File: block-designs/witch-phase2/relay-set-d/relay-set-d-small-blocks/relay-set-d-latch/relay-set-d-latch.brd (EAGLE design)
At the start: 98.8 x 51.6 mm, 58 parts, among them IC1 74LVC1G125DBV, IC10 741G175, IC11 74LVC1G17DBV, IC12 74LVC1G17DBV, IC17 74LVC1G14DBV, IC2 74LVC1G125DBV, IC3 74LVC1G125DBV, IC4 74LVC1G125DBV, IC5 74LVC1G125DBV, IC6 741G175, IC7 741G175, IC8 741G175, IC9 741G175, Q1 MMBT2907ALT1SMD, Q2 MMBT2907ALT1SMD

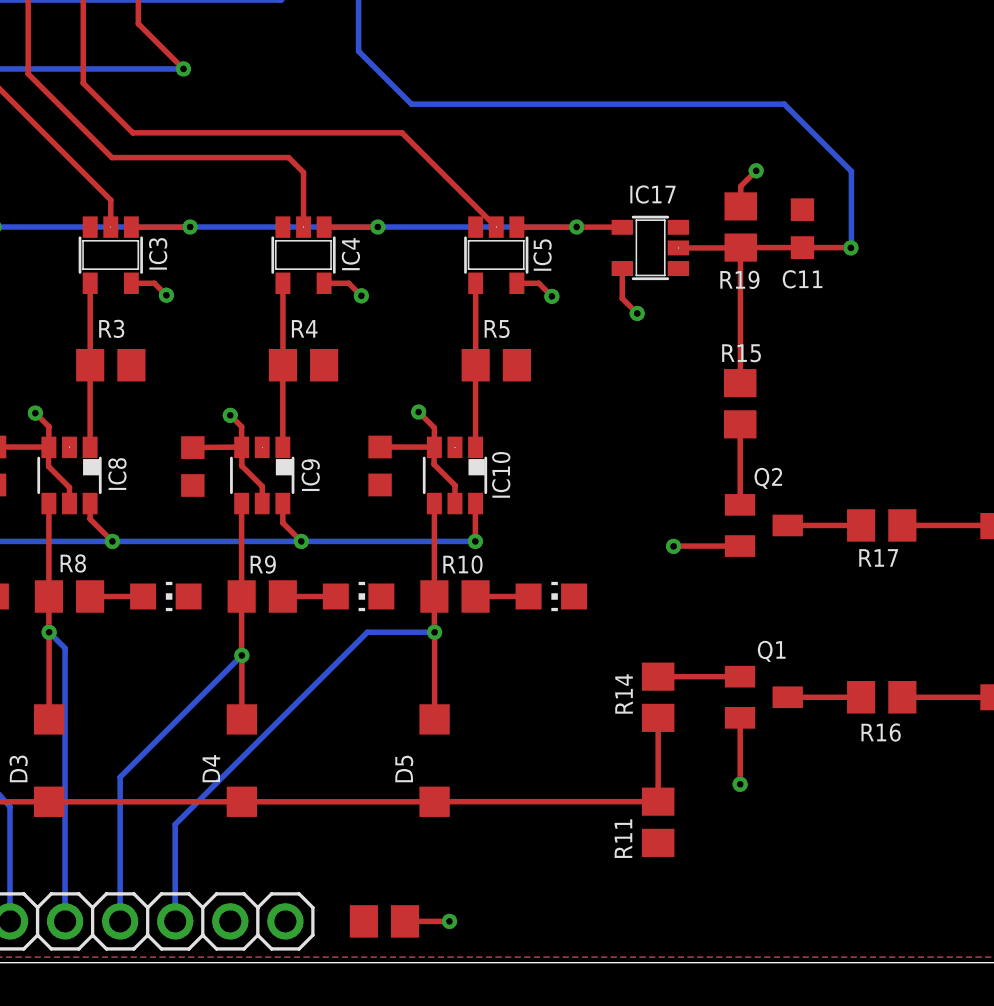
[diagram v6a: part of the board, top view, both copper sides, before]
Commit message: rework of cabling for reset, exec, power, and key-up detection
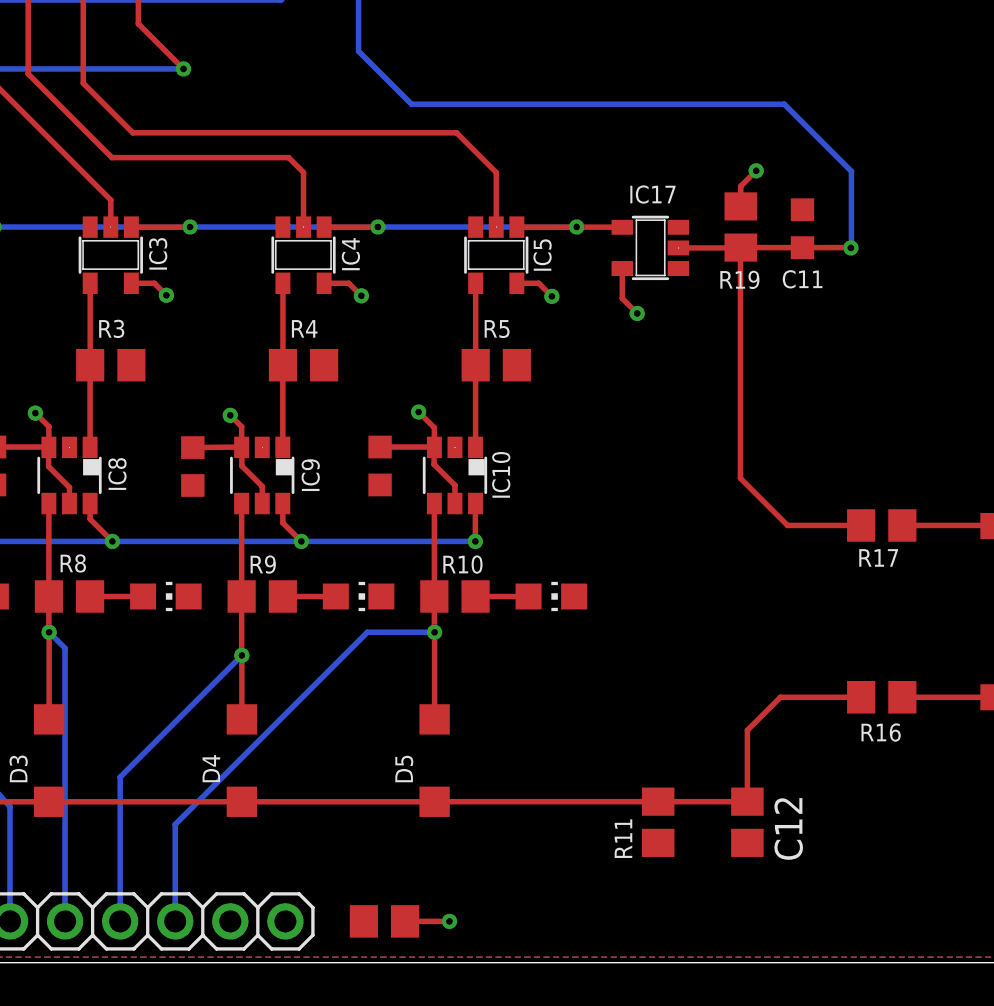
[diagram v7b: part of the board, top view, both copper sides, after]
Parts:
- removed Q1, Q2: MMBT2907ALT1SMD, transistor-pnp:SOT23-BEC
- removed R14, R15: (no value), resistor:R0805
- added C12: (no value), resistor:C0805
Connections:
- removed net N$16: Q2.B, R15.1
- removed net N$23: Q2.C, R17.1
- removed net N$25: Q1.B, R14.1
- removed net N$26: Q1.C, R16.1
- net DATA: now also C12.1, R16.1; no longer R14.2
- net GND: now also C12.2
- net SELECT: now also R17.1; no longer R15.2
- net VCC: no longer Q1.E, Q2.E
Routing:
- net SELECT: track 50.4 -> 61.3 mm
- net DATA: track 57.0 -> 66.4 mm
- net VCC: track 84.5 -> 78.3 mm, vias 18 -> 16
- net N$25: track 3.78 -> 0.00 mm
- net N$16: track 3.72 -> 0.00 mm
- net N$26: track 3.39 -> 0.00 mm
- net N$23: track 3.39 -> 0.00 mm
- net DE_IN: track 30.9 -> 32.4 mm
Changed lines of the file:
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@@
 <attribute name="VALUE" x="90.0176" y="17.6022" size="1.27" layer="27"/>
-</element>
-<element name="Q2" library="transistor-pnp" package="SOT23-BEC" value="MMBT2907ALT1SMD" x="79.6544" y="20.1676" smashed="yes" rot="R270">
-<attribute name="NAME" x="80.5942" y="22.8092" size="0.8128" layer="25" rot="R180"/>
-</element>
-<element name="R15" library="resistor" package="R0805" value="" x="78.5622" y="25.781" smashed="yes" rot="R90">
-<attribute name="NAME" x="79.6036" y="28.5242" size="0.8128" layer="25" rot="R180"/>
-<attribute name="VALUE" x="81.1022" y="25.146" size="1.27" layer="27" rot="R90"/>
 </element>
 <element name="R17" library="resistor" package="R0805" value="" x="85.09" y="20.1676" smashed="yes">
@@
 <attribute name="VALUE" x="90.0176" y="9.7028" size="1.27" layer="27"/>
 </element>
-<element name="Q1" library="transistor-pnp" package="SOT23-BEC" value="MMBT2907ALT1SMD" x="79.6544" y="12.2428" smashed="yes" rot="R270">
-<attribute name="NAME" x="80.7466" y="14.8336" size="0.8128" layer="25" rot="R180"/>
-</element>
-<element name="R14" library="resistor" package="R0805" value="" x="74.7776" y="12.2428" smashed="yes" rot="R270">
-<attribute name="NAME" x="72.7964" y="13.3604" size="0.8128" layer="25" rot="R270"/>
-<attribute name="VALUE" x="72.2376" y="12.8778" size="1.27" layer="27" rot="R270"/>
-</element>
 <element name="R16" library="resistor" package="R0805" value="" x="85.09" y="12.2428" smashed="yes">
 <attribute name="NAME" x="86.0298" y="11.0236" size="0.8128" layer="25" rot="R180"/>
@@
 <attribute name="VALUE" x="25.5524" y="33.909" size="1.27" layer="27" rot="R180"/>
 </element>
+<element name="C12" library="resistor" package="C0805" value="" x="78.8924" y="6.477" rot="R270"/>
 </elements>
 <signals>
@@
 <contactref element="C10" pad="2"/>
 <contactref element="IC12" pad="3"/>
+<contactref element="C12" pad="2"/>
 </signal>
 <signal name="DA">
@@
 </signal>
 <signal name="SELECT">
-<contactref element="R15" pad="2"/>
 <contactref element="R19" pad="2"/>
 <contactref element="C11" pad="1"/>
 <contactref element="IC17" pad="2"/>
 <via x="83.6676" y="32.9692" extent="1-16" drill="0.3048"/>
-<wire x1="78.547" y1="26.7462" x2="78.5622" y2="26.731" width="0.254" layer="1"/>
 <wire x1="75.712" y1="32.9692" x2="78.5724" y2="32.9692" width="0.254" layer="1"/>
 <wire x1="78.5876" y1="32.9844" x2="81.4324" y2="32.9832" width="0.254" layer="1"/>
@@
 <wire x1="83.693" y1="36.4998" x2="83.693" y2="32.9946" width="0.254" layer="16"/>
 <wire x1="83.693" y1="32.9946" x2="83.6676" y2="32.9692" width="0.254" layer="16"/>
-<wire x1="78.5724" y1="32.9692" x2="78.5724" y2="26.7412" width="0.254" layer="1"/>
-<wire x1="78.5724" y1="26.7412" x2="78.5622" y2="26.731" width="0.254" layer="1"/>
+<wire x1="78.5724" y1="32.9692" x2="78.5724" y2="22.3418" width="0.254" layer="1"/>
 <wire x1="60.96" y1="47.117" x2="60.96" y2="49.657" width="0.254" layer="16"/>
+<contactref element="R17" pad="1"/>
+<wire x1="78.5724" y1="22.3418" x2="80.7466" y2="20.1676" width="0.254" layer="1"/>
+<wire x1="80.7466" y1="20.1676" x2="84.14" y2="20.1676" width="0.254" layer="1"/>
 </signal>
 <signal name="!CLEAR">
@@
 <signal name="VCC">
 <contactref element="JP2" pad="1"/>
-<contactref element="Q2" pad="E"/>
-<contactref element="Q1" pad="E"/>
 <contactref element="R18" pad="2"/>
 <contactref element="IC1" pad="5"/>
@@
 <contactref element="IC17" pad="5"/>
 <contactref element="R19" pad="1"/>
-<via x="78.5622" y="8.2296" extent="1-16" drill="0.3048" diameter="0.4064"/>
-<wire x1="78.5544" y1="19.2176" x2="75.504" y2="19.2176" width="0.254" layer="1"/>
-<wire x1="75.504" y1="19.2176" x2="75.4888" y2="19.2024" width="0.254" layer="1"/>
-<via x="75.4888" y="19.2024" extent="1-16" drill="0.3048" diameter="0.4064"/>
 <wire x1="73.122" y1="32.0192" x2="73.122" y2="30.637" width="0.254" layer="1"/>
 <wire x1="73.122" y1="30.637" x2="73.8124" y2="29.9466" width="0.254" layer="1"/>
@@
 <wire x1="16.7488" y1="6.4668" x2="15.748" y2="7.4676" width="0.254" layer="1"/>
 <via x="15.748" y="7.4676" extent="1-16" drill="0.3048"/>
-<wire x1="78.5544" y1="11.2928" x2="78.5622" y2="11.285" width="0.254" layer="1"/>
-<wire x1="78.5622" y1="11.285" x2="78.5622" y2="8.2296" width="0.254" layer="1"/>
 <contactref element="JP1" pad="2"/>
 <contactref element="JP1" pad="17"/>
@@
 <contactref element="JP1" pad="12"/>
 <wire x1="48.26" y1="47.117" x2="48.26" y2="49.657" width="0.254" layer="16"/>
-<wire x1="67.31" y1="33.929" x2="62.9612" y2="38.2778" width="0.254" layer="1"/>
-<wire x1="62.9612" y1="38.2778" x2="50.546" y2="38.2778" width="0.254" layer="1"/>
+<wire x1="65.4812" y1="38.2778" x2="50.546" y2="38.2778" width="0.254" layer="1"/>
 <wire x1="50.546" y1="38.2778" x2="48.26" y2="40.5638" width="0.254" layer="1"/>
 <wire x1="48.26" y1="40.5638" x2="48.26" y2="47.117" width="0.254" layer="1"/>
-</signal>
-<signal name="N$16">
-<contactref element="R15" pad="1"/>
-<contactref element="Q2" pad="B"/>
-<wire x1="78.5622" y1="24.831" x2="78.5622" y2="21.1254" width="0.254" layer="1"/>
-<wire x1="78.5622" y1="21.1254" x2="78.5544" y2="21.1176" width="0.254" layer="1"/>
-</signal>
-<signal name="N$23">
-<contactref element="R17" pad="1"/>
-<contactref element="Q2" pad="C"/>
-<wire x1="80.7544" y1="20.1676" x2="84.14" y2="20.1676" width="0.254" layer="1"/>
+<wire x1="65.4812" y1="38.2778" x2="67.31" y2="36.449" width="0.254" layer="1"/>
+<wire x1="67.31" y1="36.449" x2="67.31" y2="33.929" width="0.254" layer="1"/>
 </signal>
 <signal name="N$24">
@@
 <wire x1="90.2122" y1="20.1676" x2="90.2376" y2="20.1422" width="0.254" layer="1"/>
 </signal>
-<signal name="N$25">
-<contactref element="R14" pad="1"/>
-<contactref element="Q1" pad="B"/>
-<wire x1="74.7776" y1="13.1928" x2="78.5544" y2="13.1928" width="0.254" layer="1"/>
-</signal>
-<signal name="N$26">
-<contactref element="R16" pad="1"/>
-<contactref element="Q1" pad="C"/>
-<wire x1="80.7544" y1="12.2428" x2="84.14" y2="12.2428" width="0.254" layer="1"/>
-</signal>
 <signal name="N$27">
 <contactref element="LED6" pad="A"/>
@@
 </signal>
 <signal name="DATA">
-<contactref element="R14" pad="2"/>
 <contactref element="D1" pad="C"/>
 <contactref element="D2" pad="C"/>
@@
 <wire x1="28.9052" y1="7.4218" x2="28.9002" y2="7.4168" width="0.254" layer="1"/>
 <wire x1="28.9002" y1="7.4168" x2="21.6608" y2="7.4168" width="0.254" layer="1"/>
-<wire x1="74.7776" y1="7.427" x2="74.7776" y2="11.2928" width="0.254" layer="1"/>
+<contactref element="R16" pad="1"/>
+<contactref element="C12" pad="1"/>
+<wire x1="74.7776" y1="7.427" x2="78.8924" y2="7.427" width="0.254" layer="1"/>
+<wire x1="78.8924" y1="7.427" x2="78.8924" y2="10.7188" width="0.254" layer="1"/>
+<wire x1="78.8924" y1="10.7188" x2="80.4164" y2="12.2428" width="0.254" layer="1"/>
+<wire x1="80.4164" y1="12.2428" x2="84.14" y2="12.2428" width="0.254" layer="1"/>
 </signal>
 <signal name="N$20">
